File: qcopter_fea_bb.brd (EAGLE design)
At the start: 50.5 x 50.8 mm, 11 parts, among them U1 ADAFRUIT_FEATHER_32U4_RFM

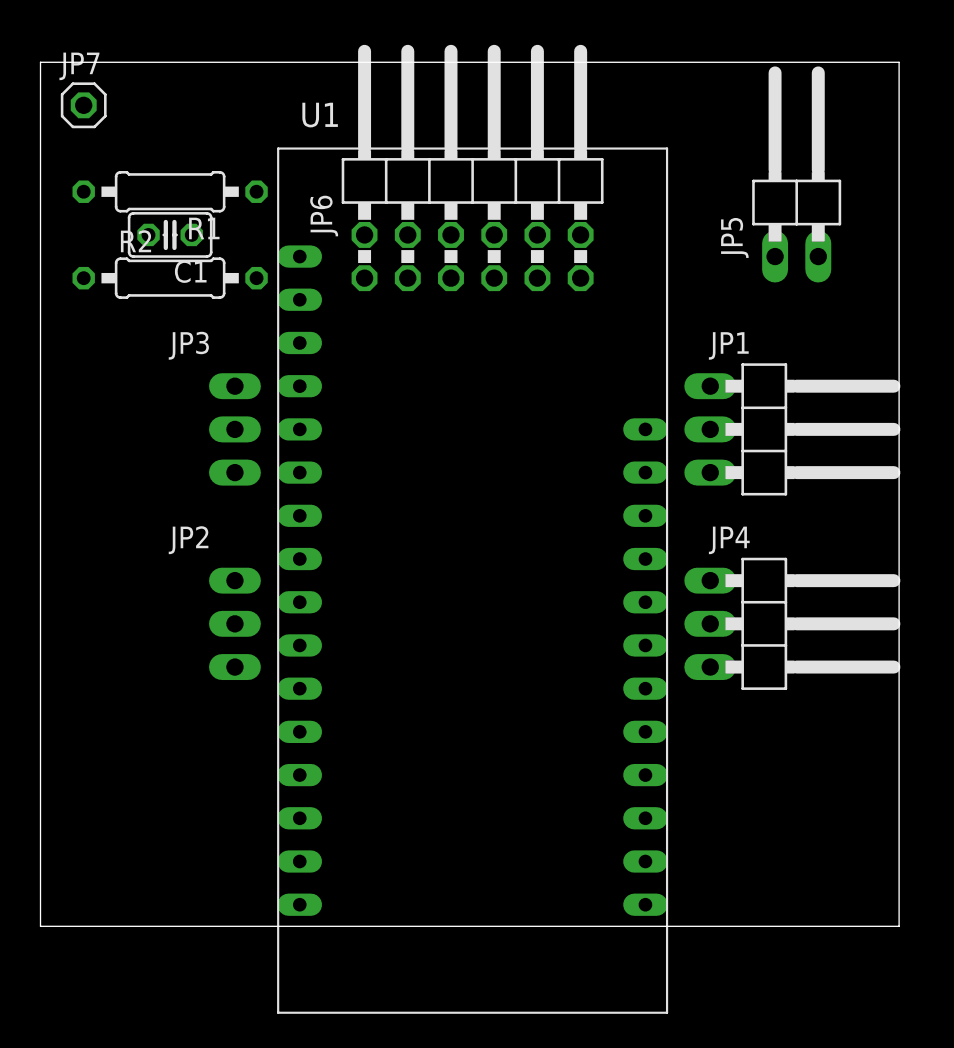
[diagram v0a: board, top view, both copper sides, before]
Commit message: Added holes 4 x 3,2mm
Added holes 4 x 3,2mm
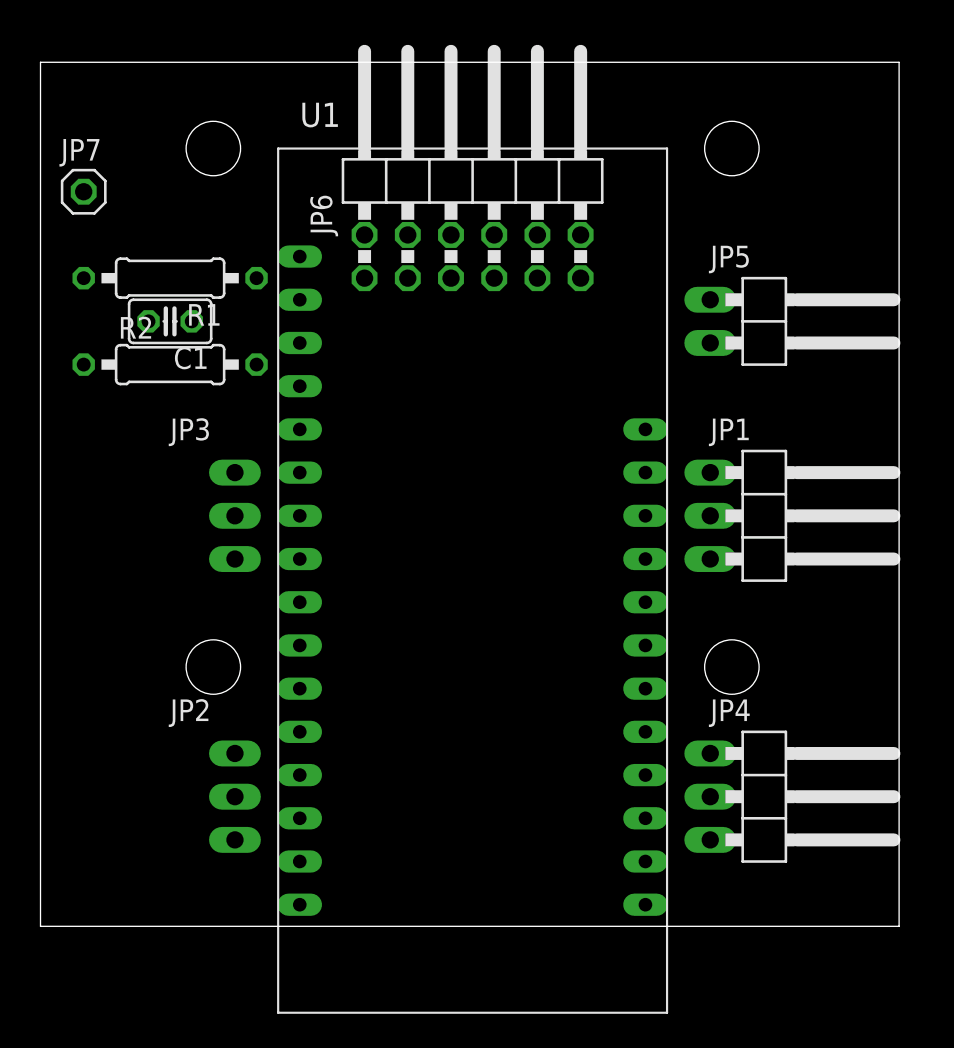
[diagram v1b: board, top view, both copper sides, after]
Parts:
- moved JP2 10.2 mm to (7.62, 7.62)
- moved JP4 10.2 mm to (43.2, 7.62)
- moved JP5 7.73 mm to (43.2, 35.6), turned to 270 degrees
- moved JP1 5.08 mm to (43.2, 24.1)
- moved JP3 5.08 mm to (7.62, 24.1)
- moved C1 5.08 mm to (7.62, 35.6)
- moved JP7 5.08 mm to (2.54, 43.2)
- moved R1 5.08 mm to (7.62, 38.1)
- moved R2 5.08 mm to (7.62, 33.0)
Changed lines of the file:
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@@
 <layer number="43" name="vRestrict" color="2" fill="10" visible="yes" active="yes"/>
 <layer number="44" name="Drills" color="7" fill="1" visible="no" active="yes"/>
-<layer number="45" name="Holes" color="7" fill="1" visible="no" active="yes"/>
+<layer number="45" name="Holes" color="7" fill="1" visible="yes" active="yes"/>
 <layer number="46" name="Milling" color="3" fill="1" visible="no" active="yes"/>
 <layer number="47" name="Measures" color="7" fill="1" visible="no" active="yes"/>
@@
 <wire x1="50.47" y1="50.79" x2="0" y2="50.79" width="0" layer="20"/>
 <wire x1="0" y1="50.79" x2="0" y2="0" width="0" layer="20"/>
+<hole x="10.16" y="45.72" drill="3.2"/>
+<hole x="40.64" y="45.72" drill="3.2"/>
+<hole x="10.16" y="15.24" drill="3.2"/>
+<hole x="40.64" y="15.24" drill="3.2"/>
 </plain>
 <attributes>
@@
 </autorouter>
 <elements>
-<element name="JP1" library="pinhead" package="1X03/90" value="" x="43.18" y="29.21" rot="R270"/>
-<element name="JP2" library="pinhead" package="1X03/90" value="" x="7.62" y="17.78" smashed="yes" rot="MR270">
-<attribute name="NAME" x="7.62" y="22.225" size="1.27" layer="25" ratio="10"/>
-<attribute name="VALUE" x="11.43" y="12.065" size="1.27" layer="28" rot="MR0"/>
+<element name="JP1" library="pinhead" package="1X03/90" value="" x="43.18" y="24.13" rot="R270"/>
+<element name="JP2" library="pinhead" package="1X03/90" value="" x="7.62" y="7.62" smashed="yes" rot="MR270">
+<attribute name="NAME" x="7.62" y="12.065" size="1.27" layer="25" ratio="10"/>
+<attribute name="VALUE" x="11.43" y="1.905" size="1.27" layer="28" rot="MR0"/>
 </element>
-<element name="JP3" library="pinhead" package="1X03/90" value="" x="7.62" y="29.21" smashed="yes" rot="MR270">
-<attribute name="NAME" x="7.62" y="33.655" size="1.27" layer="25" ratio="10"/>
-<attribute name="VALUE" x="11.43" y="23.495" size="1.27" layer="28" rot="MR0"/>
+<element name="JP3" library="pinhead" package="1X03/90" value="" x="7.62" y="24.13" smashed="yes" rot="MR270">
+<attribute name="NAME" x="7.62" y="28.575" size="1.27" layer="25" ratio="10"/>
+<attribute name="VALUE" x="11.43" y="18.415" size="1.27" layer="28" rot="MR0"/>
 </element>
-<element name="JP4" library="pinhead" package="1X03/90" value="" x="43.18" y="17.78" rot="R270"/>
-<element name="JP5" library="pinhead" package="1X02/90" value="" x="44.45" y="43.18"/>
+<element name="JP4" library="pinhead" package="1X03/90" value="" x="43.18" y="7.62" rot="R270"/>
+<element name="JP5" library="pinhead" package="1X02/90" value="" x="43.18" y="35.56" rot="R270"/>
 <element name="JP6" library="pinhead" package="2X06/90" value="Pmod NAV" x="25.4" y="44.45"/>
 <element name="U1" library="Adafruit Feather 32u4 RFM" package="ADAFRUIT_FEATHER_32U4_RFM" value="ADAFRUIT_FEATHER_32U4_RFM" x="25.4" y="19.05"/>
-<element name="R1" library="resistor" package="0207/10" value="150K" x="7.62" y="43.18" rot="R180"/>
-<element name="R2" library="resistor" package="0207/10" value="56K" x="7.62" y="38.1"/>
-<element name="C1" library="resistor" package="C025-025X050" value="0.1UF" x="7.62" y="40.64" rot="R180"/>
-<element name="JP7" library="pinhead" package="1X01" value="" x="2.54" y="48.26"/>
+<element name="R1" library="resistor" package="0207/10" value="150K" x="7.62" y="38.1" rot="R180"/>
+<element name="R2" library="resistor" package="0207/10" value="56K" x="7.62" y="33.02"/>
+<element name="C1" library="resistor" package="C025-025X050" value="0.1UF" x="7.62" y="35.56" rot="R180"/>
+<element name="JP7" library="pinhead" package="1X01" value="" x="2.54" y="43.18"/>
 </elements>
 <signals>
@@
 <contactref element="JP1" pad="3"/>
 <contactref element="U1" pad="24"/>
-<wire x1="35.56" y1="19.05" x2="39.37" y2="26.67" width="0" layer="19" extent="1-1"/>
+<wire x1="35.56" y1="19.05" x2="39.37" y2="21.59" width="0" layer="19" extent="1-1"/>
 </signal>
 <signal name="ESC2_S">
 <contactref element="U1" pad="23"/>
 <contactref element="JP2" pad="3"/>
-<wire x1="35.56" y1="16.51" x2="11.43" y2="15.24" width="0" layer="19" extent="1-1"/>
+<wire x1="35.56" y1="16.51" x2="11.43" y2="5.08" width="0" layer="19" extent="1-1"/>
 </signal>
 <signal name="ESC3_S">
 <contactref element="JP3" pad="3"/>
 <contactref element="U1" pad="22"/>
-<wire x1="35.56" y1="13.97" x2="11.43" y2="26.67" width="0" layer="19" extent="1-1"/>
+<wire x1="35.56" y1="13.97" x2="11.43" y2="21.59" width="0" layer="19" extent="1-1"/>
 </signal>
 <signal name="ESC4_S">
 <contactref element="U1" pad="21"/>
 <contactref element="JP4" pad="3"/>
-<wire x1="35.56" y1="11.43" x2="39.37" y2="15.24" width="0" layer="19" extent="1-1"/>
+<wire x1="35.56" y1="11.43" x2="39.37" y2="5.08" width="0" layer="19" extent="1-1"/>
 </signal>
 <signal name="GND">
@@
 <contactref element="R2" pad="1"/>
 <contactref element="C1" pad="2"/>
-<wire x1="39.37" y1="31.75" x2="45.72" y2="39.37" width="0" layer="19" extent="1-1"/>
-<wire x1="29.21" y1="38.1" x2="39.37" y2="31.75" width="0" layer="19" extent="1-1"/>
+<wire x1="39.37" y1="26.67" x2="39.37" y2="34.29" width="0" layer="19" extent="1-1"/>
+<wire x1="29.21" y1="38.1" x2="39.37" y2="26.67" width="0" layer="19" extent="1-1"/>
 <wire x1="29.21" y1="40.64" x2="29.21" y2="38.1" width="0" layer="19" extent="1-1"/>
-<wire x1="39.37" y1="20.32" x2="39.37" y2="31.75" width="0" layer="19" extent="1-1"/>
+<wire x1="39.37" y1="10.16" x2="39.37" y2="26.67" width="0" layer="19" extent="1-1"/>
 <wire x1="15.24" y1="31.75" x2="29.21" y2="38.1" width="0" layer="19" extent="1-1"/>
-<wire x1="11.43" y1="31.75" x2="15.24" y2="31.75" width="0" layer="19" extent="1-1"/>
-<wire x1="11.43" y1="20.32" x2="15.24" y2="31.75" width="0" layer="19" extent="1-1"/>
-<wire x1="2.54" y1="38.1" x2="11.43" y2="20.32" width="0" layer="19" extent="1-1"/>
-<wire x1="6.35" y1="40.64" x2="2.54" y2="38.1" width="0" layer="19" extent="1-1"/>
+<wire x1="11.43" y1="26.67" x2="15.24" y2="31.75" width="0" layer="19" extent="1-1"/>
+<wire x1="11.43" y1="10.16" x2="15.24" y2="31.75" width="0" layer="19" extent="1-1"/>
+<wire x1="2.54" y1="33.02" x2="11.43" y2="10.16" width="0" layer="19" extent="1-1"/>
+<wire x1="6.35" y1="35.56" x2="2.54" y2="33.02" width="0" layer="19" extent="1-1"/>
 </signal>
 <signal name="+3V3">
@@
 <contactref element="JP1" pad="2"/>
 <contactref element="JP5" pad="1"/>
-<wire x1="43.18" y1="39.37" x2="39.37" y2="29.21" width="0" layer="19" extent="1-1"/>
+<wire x1="39.37" y1="36.83" x2="39.37" y2="24.13" width="0" layer="19" extent="1-1"/>
 </signal>
 <signal name="BATT_MON">
@@
 <contactref element="U1" pad="5"/>
 <contactref element="C1" pad="1"/>
-<wire x1="12.7" y1="43.18" x2="15.24" y2="29.21" width="0" layer="19" extent="1-1"/>
-<wire x1="8.89" y1="40.64" x2="12.7" y2="43.18" width="0" layer="19" extent="1-1"/>
-<wire x1="12.7" y1="38.1" x2="8.89" y2="40.64" width="0" layer="19" extent="1-1"/>
+<wire x1="12.7" y1="38.1" x2="15.24" y2="29.21" width="0" layer="19" extent="1-1"/>
+<wire x1="8.89" y1="35.56" x2="12.7" y2="38.1" width="0" layer="19" extent="1-1"/>
+<wire x1="12.7" y1="33.02" x2="8.89" y2="35.56" width="0" layer="19" extent="1-1"/>
 </signal>
 <signal name="BATT+">
 <contactref element="JP7" pad="1"/>
 <contactref element="R1" pad="2"/>
-<wire x1="2.54" y1="43.18" x2="2.54" y2="48.26" width="0" layer="19" extent="1-1"/>
+<wire x1="2.54" y1="38.1" x2="2.54" y2="43.18" width="0" layer="19" extent="1-1"/>
 </signal>
 </signals>

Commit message: QCOPTER rev. A
QCOPTER rev. A
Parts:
- added R3, R4, R5: 100K, resistor:0207/10
- added R6: 1K, resistor:0207/10
- moved C1 0.64 mm to (8.26, 35.6)
- moved JP2 0.63 mm to (6.99, 7.62), flipped to the top, turned to 90 degrees
- moved JP3 0.63 mm to (6.99, 24.1), flipped to the top, turned to 90 degrees
- moved JP1 0.63 mm to (43.8, 24.1)
- moved JP4 0.63 mm to (43.8, 7.62)
- moved JP5 0.63 mm to (43.8, 35.6)
- moved JP6 0.63 mm to (25.4, 45.1)
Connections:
- new net N$1: JP6.5, R6.2
- net +3V3: now also R3.2, R4.2, R5.2
- net CS_A/G: now also R3.1
- net CS_ALT: now also R5.1
- net CS_M: now also R4.1
- net ESC1_S: now also JP1.1; no longer JP1.3
- net ESC4_S: now also JP4.1; no longer JP4.3
- net GND: now also JP1.3, JP4.3; no longer JP1.1, JP4.1
- net MISO: now also R6.1; no longer JP6.5
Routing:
- net INT_NAV: track 0.00 -> 55.9 mm
- net DRDY_M: track 0.00 -> 54.7 mm
- net GND: track 0.00 -> 42.9 mm, vias 0 -> 29
- net ESC3_S: track 0.00 -> 38.5 mm
- net CS_A/G: track 0.00 -> 36.1 mm
- net SCK: track 0.00 -> 35.3 mm
- net ESC2_S: track 0.00 -> 32.3 mm
- net CS_ALT: track 0.00 -> 29.9 mm
- net MOSI: track 0.00 -> 29.9 mm
- net CS_M: track 0.00 -> 26.3 mm
- net +3V3: track 0.00 -> 26.3 mm
- net MISO: track 0.00 -> 19.2 mm
- net BEC_+5V: track 0.00 -> 18.3 mm
- net BATT_MON: track 0.00 -> 13.1 mm
- net ESC1_S: track 0.00 -> 11.3 mm
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- added copper zone on layer 1, net GND
- added copper zone on layer 16, net GND
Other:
- board text added: "+5V GND"
- board text added: "1"
- board text added: "16"
- board text added: "17"
- board text added: "28"
- board text added: "5V OUT"
- board text added: "BATT+"
- board text added: "ESC1"
- board text added: "ESC2"
- board text added: "ESC3"
- board text added: "ESC4"
- board text added: "QCOPTER rev. A"
- board text added: "S +5V GND"
- board text added: "S GND"

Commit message: R1, R2 = 100K, C1 = 0,33F
R1, R2 = 100K, C1 = 0,33F
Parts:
- C1: value 0.1UF -> 0.33UF
- R1: value 150K -> 100K
- R2: value 56K -> 10K
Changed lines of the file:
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@@
 <attribute name="NAME" x="14.605" y="46.355" size="1.4224" layer="25"/>
 </element>
-<element name="R1" library="resistor" package="0207/10" value="150K" x="7.62" y="38.1" smashed="yes" rot="R180">
+<element name="R1" library="resistor" package="0207/10" value="100K" x="7.62" y="38.1" smashed="yes" rot="R180">
 <attribute name="NAME" x="4.318" y="40.386" size="1.27" layer="25" ratio="10" rot="R180"/>
 <attribute name="VALUE" x="9.8806" y="38.735" size="1.27" layer="27" ratio="10" rot="R180"/>
 </element>
-<element name="R2" library="resistor" package="0207/10" value="56K" x="7.62" y="33.02" smashed="yes">
+<element name="R2" library="resistor" package="0207/10" value="10K" x="7.62" y="33.02" smashed="yes">
 <attribute name="NAME" x="2.032" y="33.909" size="1.27" layer="25" ratio="10"/>
 <attribute name="VALUE" x="5.3594" y="32.385" size="1.27" layer="27" ratio="10"/>
 </element>
-<element name="C1" library="resistor" package="C025-025X050" value="0.1UF" x="8.255" y="35.56" smashed="yes" rot="R180">
+<element name="C1" library="resistor" package="C025-025X050" value="0.33UF" x="8.255" y="35.56" smashed="yes" rot="R180">
 <attribute name="NAME" x="13.081" y="35.941" size="1.27" layer="25" ratio="10" rot="R180"/>
 <attribute name="VALUE" x="10.541" y="38.354" size="1.27" layer="27" ratio="10" rot="R180"/>
